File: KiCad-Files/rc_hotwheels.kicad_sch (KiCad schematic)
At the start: 13 parts, among them IC1 BD6211F-E2, IC2 MIC5504-3.3YM5-TR, U1 STM32F070F6P6, U3 NRF24L01_Breakout

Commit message: Updated MCU footprint
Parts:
- IC1: footprint SOIC127P620X171-8N -> BD6211F-E2:SOIC127P620X171-8N
- IC2: footprint SOT95P280X145-5N -> MIC5504-3.3YM5-TR:SOT95P280X145-5N
- U1: footprint TSSOP20 -> STM32F070F6P6:SOP65P640X120-20N
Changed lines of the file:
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@@
       (effects (font (size 1.27 1.27)))
     )
-    (property "Footprint" "SOT95P280X145-5N" (at 66.04 85.09 0)
+    (property "Footprint" "MIC5504-3.3YM5-TR:SOT95P280X145-5N" (at 66.04 85.09 0)
       (effects (font (size 1.27 1.27)) (justify left) hide)
     )
@@
       (effects (font (size 1.524 1.524)))
     )
-    (property "Footprint" "TSSOP20" (at 31.75 39.37 0)
+    (property "Footprint" "STM32F070F6P6:SOP65P640X120-20N" (at 31.75 39.37 0)
       (effects (font (size 1.27 1.27) italic) hide)
     )
@@
       (effects (font (size 1.524 1.524)))
     )
-    (property "Footprint" "TSSOP20" (at 207.01 39.37 0)
+    (property "Footprint" "STM32F070F6P6:SOP65P640X120-20N" (at 207.01 39.37 0)
       (effects (font (size 1.27 1.27) italic) hide)
     )
@@
       (effects (font (size 1.27 1.27)))
     )
-    (property "Footprint" "SOIC127P620X171-8N" (at 69.85 266.37 0)
+    (property "Footprint" "BD6211F-E2:SOIC127P620X171-8N" (at 69.85 266.37 0)
       (effects (font (size 1.27 1.27)) (justify left top) hide)
     )

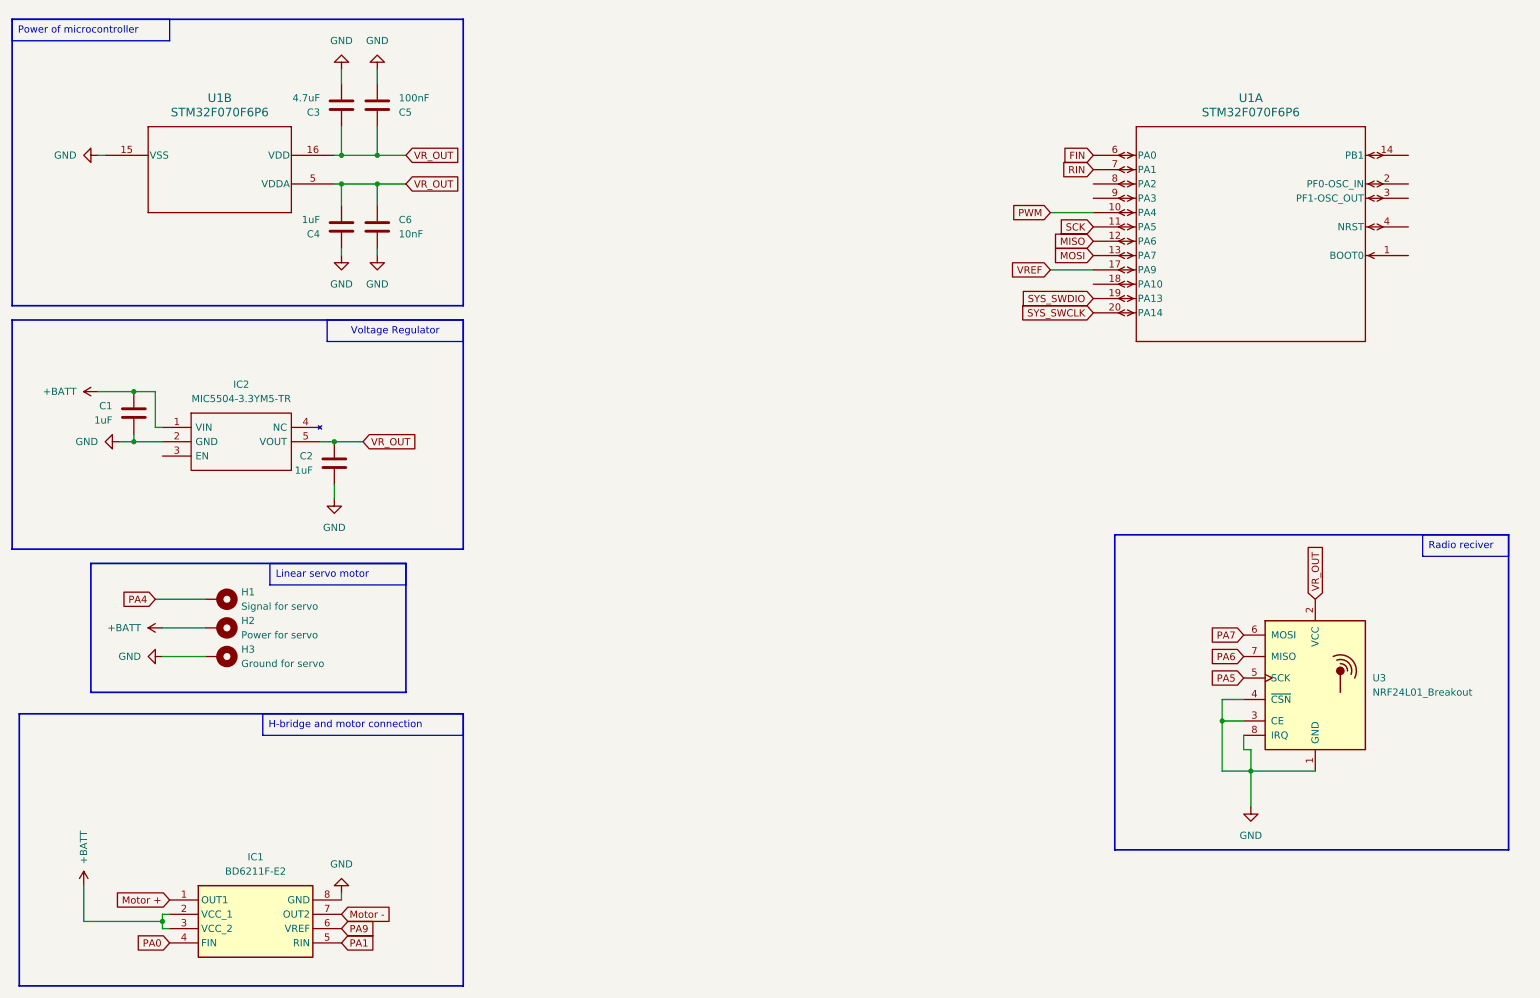
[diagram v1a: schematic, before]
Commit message: Created PCB Design
 - Placed Components at the right place. Connected Voltage Regulator chip to MCU.
- Changed Capacitors Footprint and Symbol.
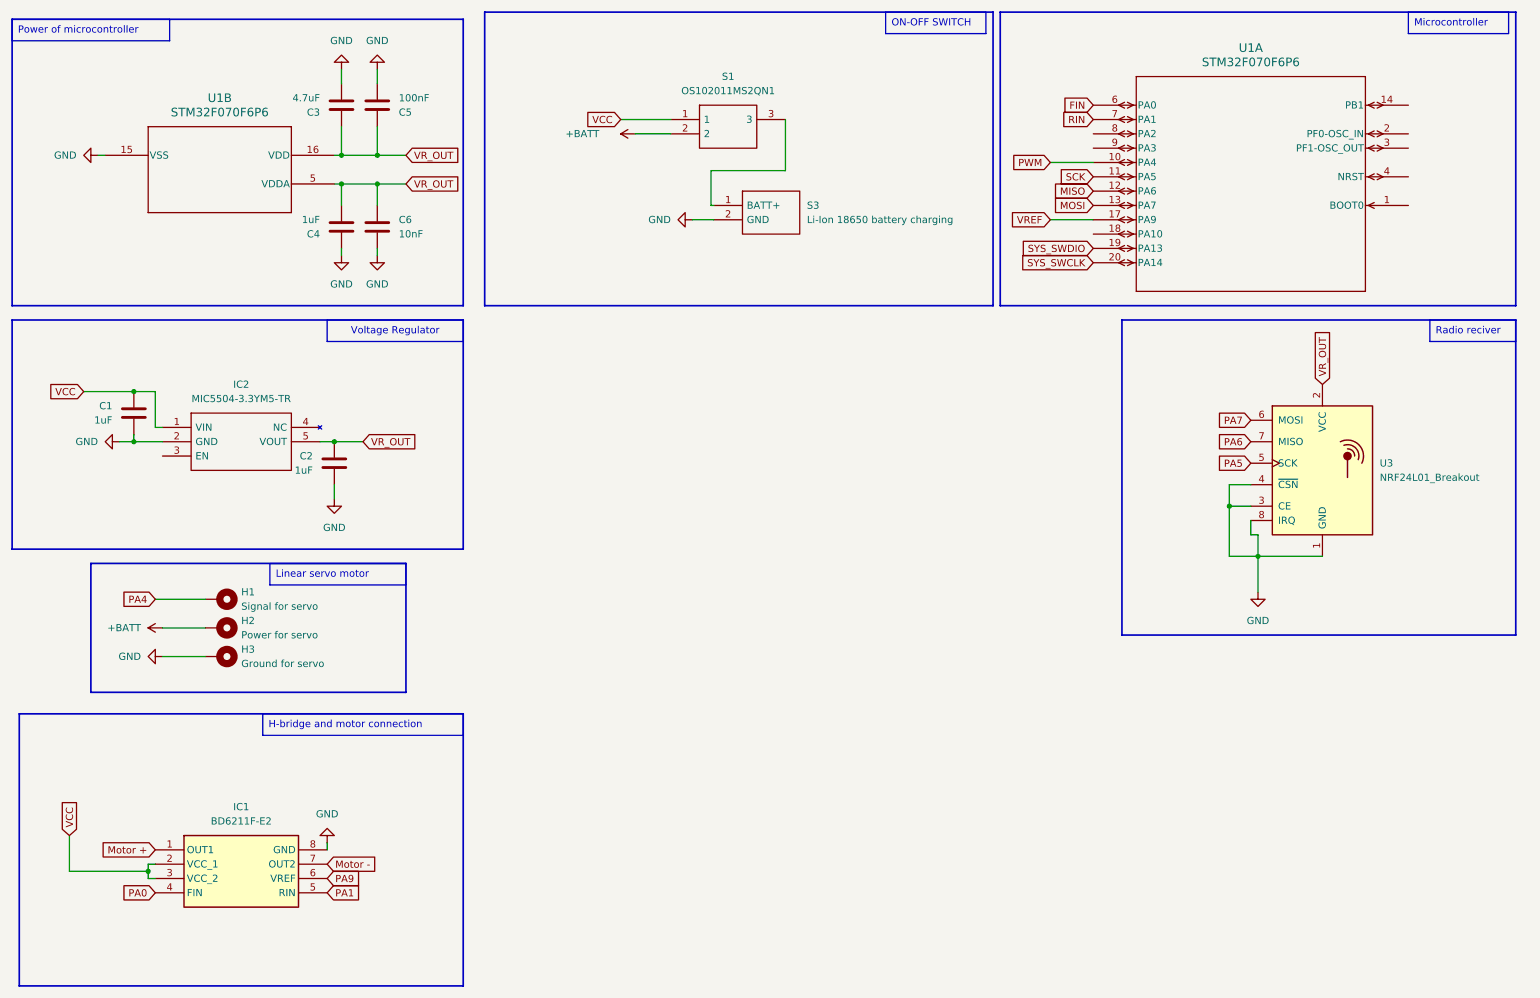
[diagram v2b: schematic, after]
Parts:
- added S1: OS102011MS2QN1, OS102011MA1QN1, symbol OS102011MS2QN1:OS102011MS2QN1
- added S3: Li-Ion 18650 battery charging, OS102011MA1QN1, symbol OS102011MS2QN1:OS102011MS2QN1
- C1, C2, C4: footprint Capacitor_THT:C_Rect_L4.6mm_W2.0mm_P2.50mm_MKS02_FKP02 -> C1uF:CAPC1005X55N
- C3: footprint Capacitor_THT:C_Rect_L4.6mm_W2.0mm_P2.50mm_MKS02_FKP02 -> C4.7uF:CAPC1608X87N
- C5: footprint Capacitor_THT:C_Rect_L4.6mm_W2.0mm_P2.50mm_MKS02_FKP02 -> C100nF:CAPC1005X55N
- C6: footprint Capacitor_THT:C_Rect_L4.6mm_W2.0mm_P2.50mm_MKS02_FKP02 -> C10nF:CAPC1005X55N
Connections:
- net +BATT: now also S1.2; no longer C1.2, IC1.2 (VCC_1), IC1.3 (VCC_2), IC2.1 (VIN)
- net GND: now also S3.2 (GND)
- new net: S1.3, S3.1 (BATT+)
- new net VCC: C1.2, IC1.2 (VCC_1), IC1.3 (VCC_2), IC2.1 (VIN), S1.1
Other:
- moved on the sheet: IC1, U1A, U3

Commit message: Fixed all schematic errors.
Co-Authored-By: Yazid Almazroua <98489302+yazidta@users.noreply.github.com>
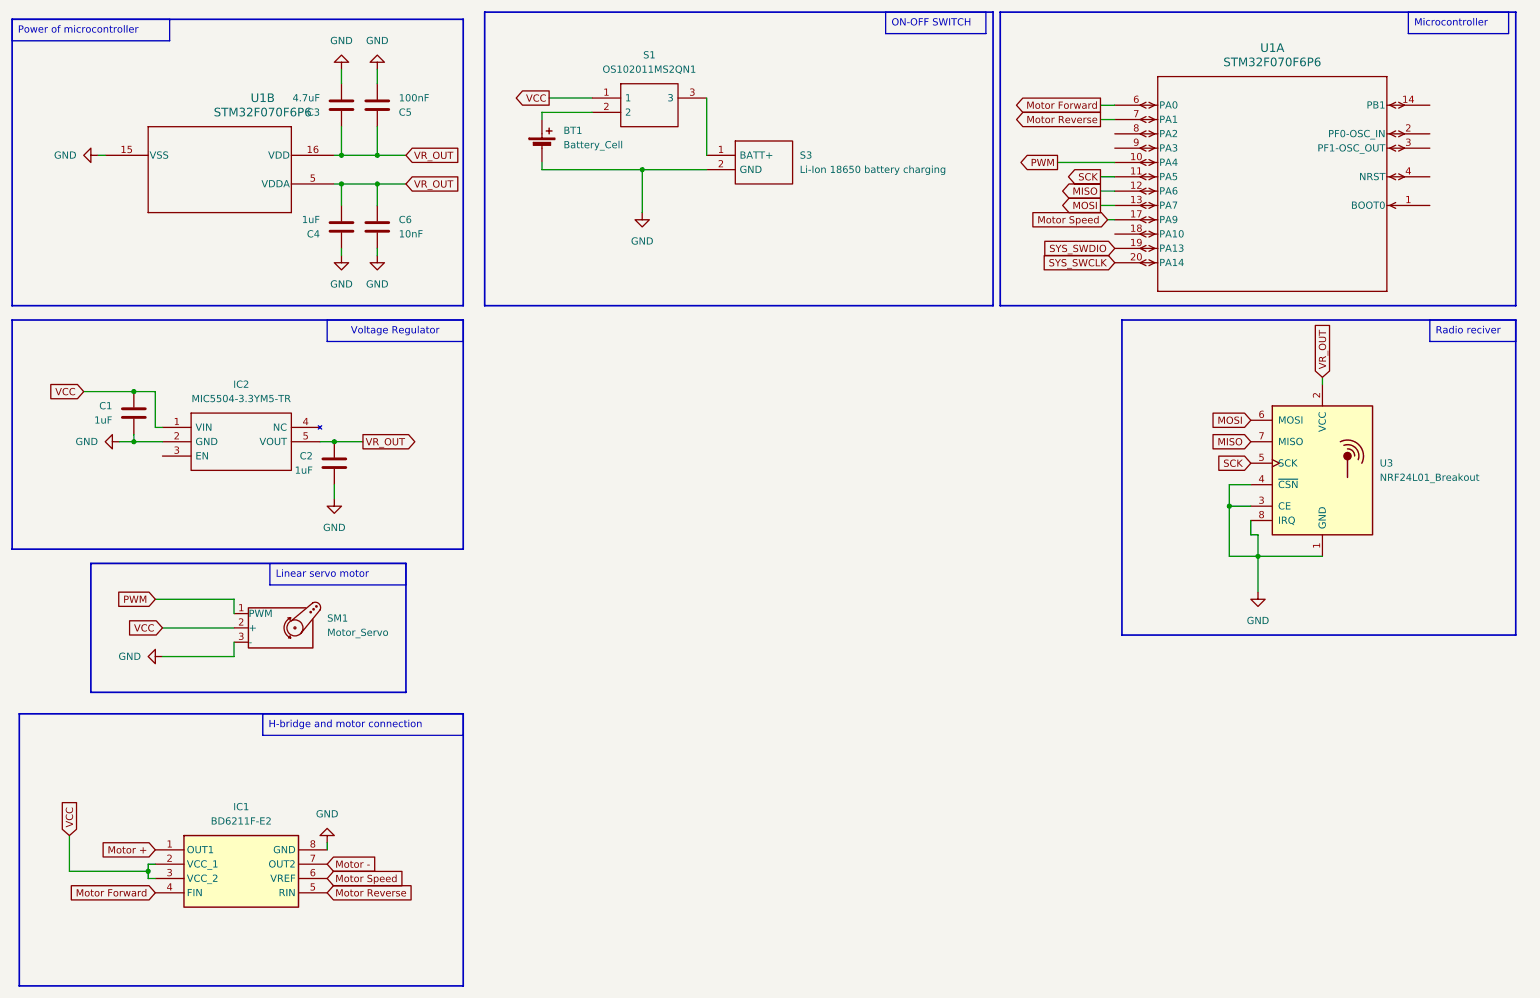
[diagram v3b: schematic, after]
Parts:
- removed H1: Signal for servo, MountingHole:MountingHole_2.2mm_M2_DIN965_Pad, symbol Mechanical:MountingHole_Pad
- removed H2: Power for servo, MountingHole:MountingHole_2.2mm_M2_DIN965_Pad, symbol Mechanical:MountingHole_Pad
- removed H3: Ground for servo, MountingHole:MountingHole_2.2mm_M2_DIN965_Pad, symbol Mechanical:MountingHole_Pad
- added BT1: Battery_Cell, symbol Device:Battery_Cell
- added SM1: Motor_Servo, symbol Motor:Motor_Servo
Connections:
- net PA0 is gone; now on net Motor Forward: IC1.4 (FIN)
- net PA5 is gone; now on net SCK: U3.5 (SCK)
- net PA6 is gone; now on net MISO: U3.7 (MISO)
- net PA7 is gone; now on net MOSI: U3.6 (MOSI)
- net RIN is gone; now on net Motor Reverse: U1.7 (PA1)
- net VREF is gone; now on net Motor Speed: U1.17 (PA9)
- net PWM: now also SM1.1 (PWM)
- net VCC: now also SM1.2 (+)
- net +BATT: no longer names the net of S1.2
- net +BATT: now also BT1.1 (+)
- net FIN renamed Motor Forward
- removed net GND: C1.1, C2.1, C3.1, C4.2, C5.1, C6.1, IC1.8 (GND), IC2.2 (GND), S3.2 (GND), U1.15 (VSS), U3.1 (GND), U3.3 (CE), U3.4 (~{CSN}), U3.8 (IRQ)
- net PA1 renamed Motor Reverse
- net PA9 renamed Motor Speed
- new net: U3.1 (GND), U3.3 (CE), U3.4 (~{CSN}), U3.8 (IRQ)
- new net: C1.1, IC2.2 (GND)
- new net: BT1.2 (-), S3.2 (GND)
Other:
- moved on the sheet: S1, S3, U1A

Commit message: PCB V2.0
Co-Authored-By: Yazid Almazroua <98489302+yazidta@users.noreply.github.com>
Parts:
- BT1: footprint (none) -> Library:Battery_Pads
- S3: footprint OS102011MA1QN1 -> Library:Battery_Pads
- SM1: footprint (none) -> Library:Servo_Motor
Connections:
- net Motor Forward: now also U1.7 (PA1); no longer U1.6 (PA0)
- net Motor Reverse: now also U1.6 (PA0); no longer U1.7 (PA1)
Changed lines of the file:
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@@
     )
   )
-  (global_label "Motor Reverse" (shape output) (at 208.28 33.02 180) (fields_autoplaced)
-    (effects (font (size 1.27 1.27)) (justify right))
-    (property "Intersheetrefs" "${INTERSHEET_REFS}" (at 191.7482 33.02 0)
-      (effects (font (size 1.27 1.27)) (justify right) hide)
-    )
-    (property "RIN" "" (at 208.28 35.2108 0)
+  (global_label "Motor Forward" (shape output) (at 208.28 33.02 180) (fields_autoplaced)
+    (effects (font (size 1.27 1.27)) (justify right))
+    (property "Intersheetrefs" "${INTERSHEET_REFS}" (at 191.6274 33.02 0)
+      (effects (font (size 1.27 1.27)) (justify right) hide)
+    )
+    (property "FIN" "" (at 208.28 35.2108 0)
       (effects (font (size 1.27 1.27)) (justify right) hide)
     )
@@
     )
   )
-  (global_label "Motor Forward" (shape output) (at 208.28 30.48 180) (fields_autoplaced)
-    (effects (font (size 1.27 1.27)) (justify right))
-    (property "Intersheetrefs" "${INTERSHEET_REFS}" (at 191.6274 30.48 0)
-      (effects (font (size 1.27 1.27)) (justify right) hide)
-    )
-    (property "FIN" "" (at 208.28 32.6708 0)
+  (global_label "Motor Reverse" (shape output) (at 208.28 30.48 180) (fields_autoplaced)
+    (effects (font (size 1.27 1.27)) (justify right))
+    (property "Intersheetrefs" "${INTERSHEET_REFS}" (at 191.7482 30.48 0)
+      (effects (font (size 1.27 1.27)) (justify right) hide)
+    )
+    (property "RIN" "" (at 208.28 32.6708 0)
       (effects (font (size 1.27 1.27)) (justify right) hide)
     )
@@
     (pin "1")
     (pin "2")
-    (pin "3")
     (pin "4")
     (pin "5")
+    (pin "3")
     (instances
       (project "rc_hotwheels"
@@
       (effects (font (size 1.27 1.27)) (justify left))
     )
-    (property "Footprint" "OS102011MA1QN1" (at 154.94 36.83 0)
+    (property "Footprint" "Library:Battery_Pads" (at 154.94 36.83 0)
       (effects (font (size 1.27 1.27)) (justify left) hide)
     )
@@
       (effects (font (size 1.27 1.27)) (justify left))
     )
-    (property "Footprint" "" (at 109.22 36.576 90)
+    (property "Footprint" "Library:Battery_Pads" (at 109.22 36.576 90)
       (effects (font (size 1.27 1.27)) hide)
     )
@@
       (effects (font (size 1.27 1.27)) (justify left))
     )
-    (property "Footprint" "" (at 62.23 128.016 0)
-      (effects (font (size 1.27 1.27)) hide)
-    )
+    (property "Footprint" "Library:Servo_Motor" (at 62.23 128.016 0)
+      (effects (font (size 1.27 1.27)) hide)
+    )

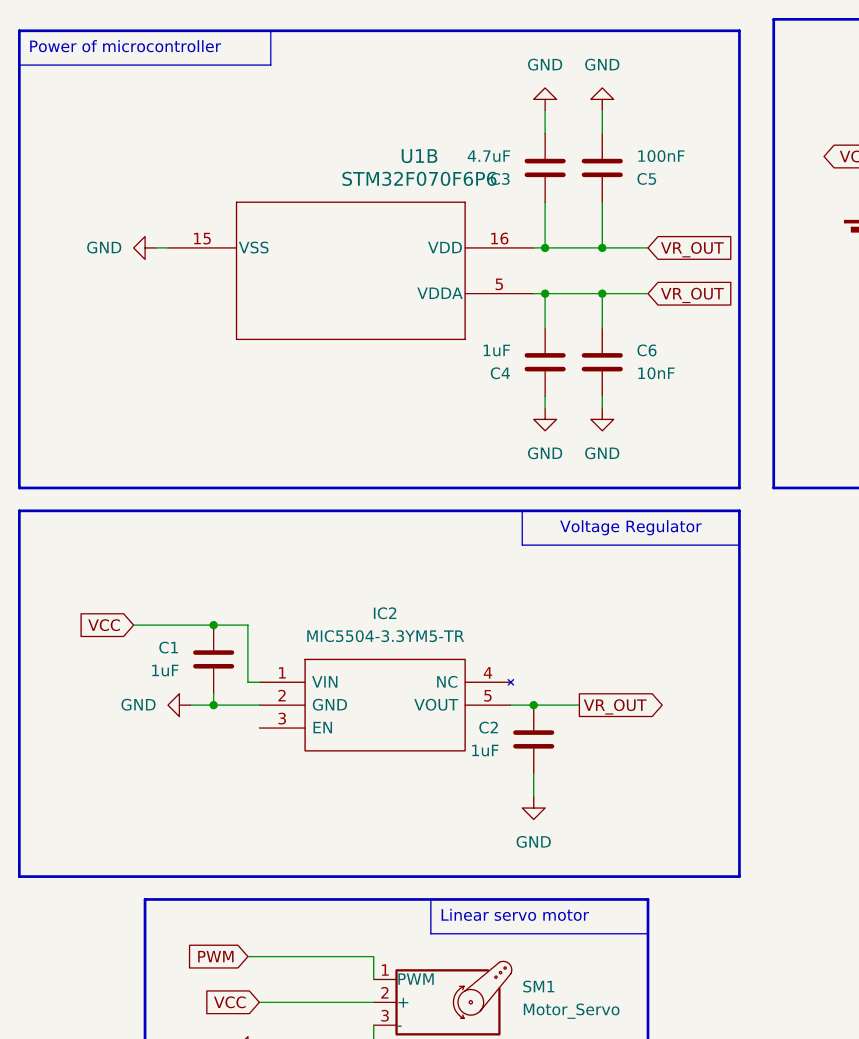
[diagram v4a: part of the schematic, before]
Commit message: Updated Capcitors libs
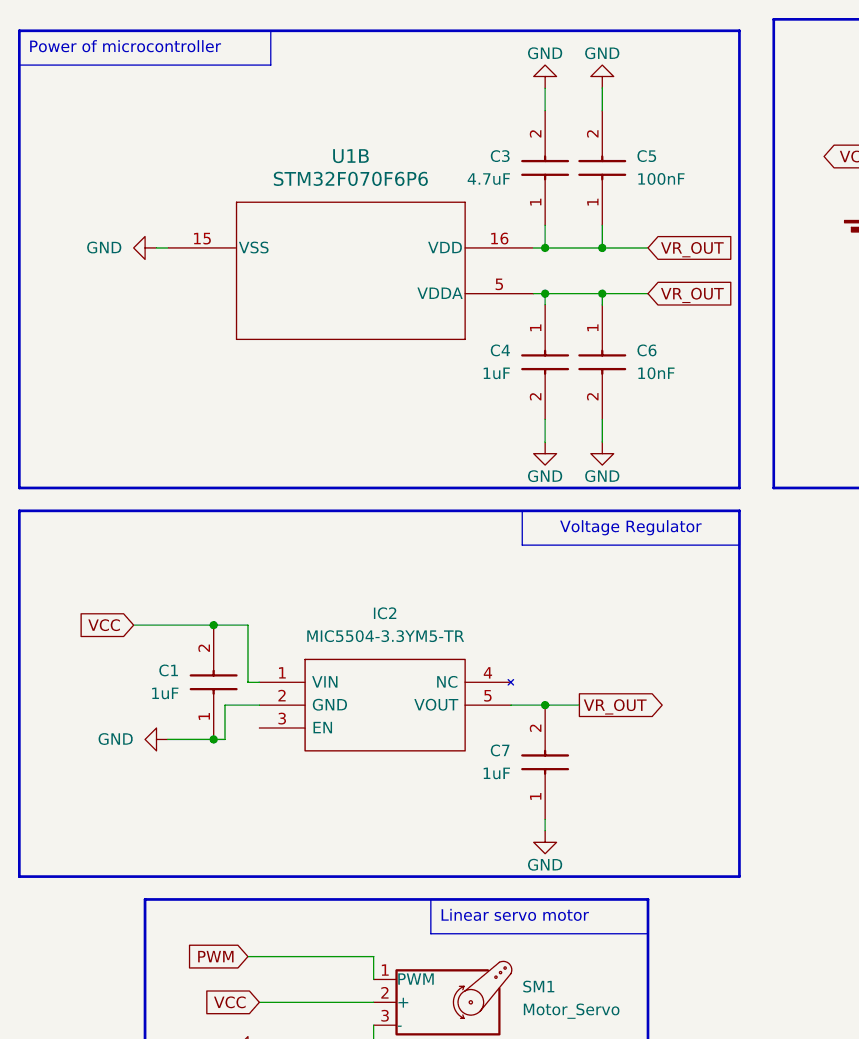
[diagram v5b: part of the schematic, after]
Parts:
- removed C1, C2, C4: 1uF, C1uF:CAPC1005X55N, symbol Device:C
- removed C3: 4.7uF, C4.7uF:CAPC1608X87N, symbol Device:C
- removed C5: 100nF, C100nF:CAPC1005X55N, symbol Device:C
- removed C6: 10nF, C10nF:CAPC1005X55N, symbol Device:C
- added C1, C4, C7: 1uF, CAPC3225X105N, symbol 885012209003:885012209003
- added C3: 4.7uF, CAPC3225X220N, symbol 885012209004:885012209004
- added C5: 100nF, CAPC3225X105N, symbol 885012209041:885012209041
- added C6: 10nF, CAPC3225X105N, symbol 885012209035:885012209035
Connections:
- net VCC: now also C1.2
- net VR_OUT: now also C3.1, C4.1, C5.1, C6.1, C7.2
- net at IC2.2 (GND): now also C1.1
